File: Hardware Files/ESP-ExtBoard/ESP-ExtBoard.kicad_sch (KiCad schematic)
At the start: 6 parts, among them J1 PIN_HEADER, J2 PIN_HEADER_1x4, U1 ESP32-DEVKIT-V1, U2 BME280, U3 MPU6050, U4 SSD1306

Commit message: Signed-off-by: Freire <freireg1503@gmail.com>
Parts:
- added J3: PIN_HEADER, New_lib:PinHeader_1x06_P2.54mm_Vertical, symbol New_Library:PIN_HEADER_1x6
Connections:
- net +3.3V: now also J3.1
- net Earth: now also J3.2
- net GPIO25: now reaches U1.23 (D25)
- net GPIO25: now also J3.6
- net GPIO26: now reaches U1.24 (D26)
- net GPIO26: now also J3.5
- net GPIO27: now reaches U1.25 (D27)
- net GPIO27: now also J3.4
- net GPIO14: now reaches U1.26 (D14)
- net GPIO14: now also J3.3
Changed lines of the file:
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@@
+    (stroke (width 0) (type default))
+  )
+  (wire (pts (xy 88.9 91.44) (xy 86.36 91.44))
+    (stroke (width 0) (type default))
+  )
+  (wire (pts (xy 115.57 139.7) (xy 118.11 139.7))
+    (stroke (width 0) (type default))
+  )
+  (wire (pts (xy 114.3 149.86) (xy 118.11 149.86))
     (stroke (width 0) (type default))
   )
@@
     (stroke (width 0) (type default))
   )
+  (wire (pts (xy 115.57 147.32) (xy 118.11 147.32))
+    (stroke (width 0) (type default))
+  )
   (wire (pts (xy 114.3 113.03) (xy 118.11 113.03))
     (stroke (width 0) (type default))
   )
+  (wire (pts (xy 52.07 96.52) (xy 55.88 96.52))
+    (stroke (width 0) (type default))
+  )
   (wire (pts (xy 115.57 133.35) (xy 118.11 133.35))
     (stroke (width 0) (type default))
@@
     (stroke (width 0) (type default))
   )
+  (wire (pts (xy 115.57 152.4) (xy 118.11 152.4))
+    (stroke (width 0) (type default))
+  )
   (wire (pts (xy 86.36 115.57) (xy 86.36 111.76))
     (stroke (width 0) (type default))
@@
     (stroke (width 0) (type default))
   )
+  (wire (pts (xy 115.57 142.24) (xy 118.11 142.24))
+    (stroke (width 0) (type default))
+  )
   (wire (pts (xy 114.3 130.81) (xy 118.11 130.81))
     (stroke (width 0) (type default))
@@
     (stroke (width 0) (type default))
   )
+  (wire (pts (xy 88.9 93.98) (xy 86.36 93.98))
+    (stroke (width 0) (type default))
+  )
+  (wire (pts (xy 88.9 88.9) (xy 86.36 88.9))
+    (stroke (width 0) (type default))
+  )
+  (wire (pts (xy 115.57 144.78) (xy 118.11 144.78))
+    (stroke (width 0) (type default))
+  )
   (wire (pts (xy 118.11 92.71) (xy 114.3 92.71))
     (stroke (width 0) (type default))
@@
   (label "VSPI_MISO" (at 115.57 125.73 180) (fields_autoplaced)
     (effects (font (size 1.27 1.27)) (justify right bottom))
+  )
+  (label "GPIO26" (at 88.9 91.44 0) (fields_autoplaced)
+    (effects (font (size 1.27 1.27)) (justify left bottom))
   )
   (label "UART2_RX" (at 88.9 76.2 0) (fields_autoplaced)
@@
     (effects (font (size 1.27 1.27)) (justify right bottom))
   )
+  (label "GPIO14" (at 115.57 147.32 180) (fields_autoplaced)
+    (effects (font (size 1.27 1.27)) (justify right bottom))
+  )
+  (label "GPIO27" (at 88.9 93.98 0) (fields_autoplaced)
+    (effects (font (size 1.27 1.27)) (justify left bottom))
+  )
+  (label "GPIO26" (at 115.57 142.24 180) (fields_autoplaced)
+    (effects (font (size 1.27 1.27)) (justify right bottom))
+  )
   (label "VSPI_CLK" (at 114.3 123.19 180) (fields_autoplaced)
     (effects (font (size 1.27 1.27)) (justify right bottom))
@@
     (effects (font (size 1.27 1.27)) (justify right bottom))
   )
+  (label "GPIO25" (at 88.9 88.9 0) (fields_autoplaced)
+    (effects (font (size 1.27 1.27)) (justify left bottom))
+  )
+  (label "GPIO14" (at 52.07 96.52 180) (fields_autoplaced)
+    (effects (font (size 1.27 1.27)) (justify right bottom))
+  )
   (label "VSPI_MOSI" (at 88.9 86.36 0) (fields_autoplaced)
     (effects (font (size 1.27 1.27)) (justify left bottom))
@@
     (effects (font (size 1.27 1.27)) (justify left bottom))
   )
+  (label "GPIO27" (at 115.57 144.78 180) (fields_autoplaced)
+    (effects (font (size 1.27 1.27)) (justify right bottom))
+  )
   (label "VSPI_CS" (at 50.8 88.9 180) (fields_autoplaced)
     (effects (font (size 1.27 1.27)) (justify right bottom))
@@
   )
   (label "I2C0_SCL" (at 114.3 92.71 180) (fields_autoplaced)
+    (effects (font (size 1.27 1.27)) (justify right bottom))
+  )
+  (label "GPIO25" (at 115.57 139.7 180) (fields_autoplaced)
     (effects (font (size 1.27 1.27)) (justify right bottom))
   )
@@
         (path "/1974cf77-3075-4097-b9ae-5746e4e11ede"
           (reference "U2") (unit 1)
+        )
+      )
+    )
+  )
+  (symbol (lib_id "power:+3.3V") (at 115.57 152.4 90) (unit 1)
+    (in_bom yes) (on_board yes) (dnp no) (fields_autoplaced)
+    (property "Reference" "#PWR014" (at 119.38 152.4 0)
+      (effects (font (size 1.27 1.27)) hide)
+    )
+    (property "Value" "+3.3V" (at 110.49 152.4 0)
+      (effects (font (size 1.27 1.27)))
+    )
+    (property "Footprint" "" (at 115.57 152.4 0)
+      (effects (font (size 1.27 1.27)) hide)
+    )
+    (property "Datasheet" "" (at 115.57 152.4 0)
+      (effects (font (size 1.27 1.27)) hide)
+    )
+    (pin "1")
+    (instances
+      (project "ESP-ExtBoard"
+        (path "/1974cf77-3075-4097-b9ae-5746e4e11ede"
+          (reference "#PWR014") (unit 1)
         )
       )
@@
     )
   )
-  (symbol (lib_id "New_Library:SSD1306") (at 127 109.22 90) (unit 1)
-    (in_bom yes) (on_board yes) (dnp no) (fields_autoplaced)
-    (property "Reference" "U4" (at 134.62 107.95 90)
-      (effects (font (size 1.27 1.27)) (justify right))
-    )
-    (property "Value" "SSD1306" (at 134.62 110.49 90)
-      (effects (font (size 1.27 1.27)) (justify right))
-    )
-    (property "Footprint" "New_lib:128x64OLED" (at 120.65 109.22 0)
-      (effects (font (size 1.27 1.27)) hide)
-    )
-    (property "Datasheet" "" (at 120.65 109.22 0)
+  (symbol (lib_id "New_Library:PIN_HEADER_1x6") (at 124.46 147.32 90) (unit 1)
+    (in_bom yes) (on_board yes) (dnp no) (fields_autoplaced)
+    (property "Reference" "J3" (at 128.27 146.05 90)
+      (effects (font (size 1.27 1.27)) (justify right))
+    )
+    (property "Value" "PIN_HEADER" (at 128.27 148.59 90)
+      (effects (font (size 1.27 1.27)) (justify right))
+    )
+    (property "Footprint" "New_lib:PinHeader_1x06_P2.54mm_Vertical" (at 128.27 148.59 0)
+      (effects (font (size 1.27 1.27)) hide)
+    )
+    (property "Datasheet" "" (at 124.46 148.59 0)
       (effects (font (size 1.27 1.27)) hide)
     )
@@
     (pin "3")
     (pin "4")
+    (pin "5")
+    (pin "6")
+    (instances
+      (project "ESP-ExtBoard"
+        (path "/1974cf77-3075-4097-b9ae-5746e4e11ede"
+          (reference "J3") (unit 1)
+        )
+      )
+    )
+  )
+  (symbol (lib_id "New_Library:SSD1306") (at 127 109.22 90) (unit 1)
+    (in_bom yes) (on_board yes) (dnp no) (fields_autoplaced)
+    (property "Reference" "U4" (at 134.62 107.95 90)
+      (effects (font (size 1.27 1.27)) (justify right))
+    )
+    (property "Value" "SSD1306" (at 134.62 110.49 90)
+      (effects (font (size 1.27 1.27)) (justify right))
+    )
+    (property "Footprint" "New_lib:128x64OLED" (at 120.65 109.22 0)
+      (effects (font (size 1.27 1.27)) hide)
+    )
+    (property "Datasheet" "" (at 120.65 109.22 0)
+      (effects (font (size 1.27 1.27)) hide)
+    )
+    (pin "1")
+    (pin "2")
+    (pin "3")
+    (pin "4")
     (instances
       (project "ESP-ExtBoard"
@@
         )
       )
+    )
+  )
+  (symbol (lib_id "power:Earth") (at 114.3 149.86 270) (unit 1)
+    (in_bom yes) (on_board yes) (dnp no) (fields_autoplaced)
+    (property "Reference" "#PWR013" (at 107.95 149.86 0)
+      (effects (font (size 1.27 1.27)) hide)
+    )
+    (property "Value" "Earth" (at 110.49 149.86 0)
+      (effects (font (size 1.27 1.27)) hide)
+    )
+    (property "Footprint" "" (at 114.3 149.86 0)
+      (effects (font (size 1.27 1.27)) hide)
+    )
+    (property "Datasheet" "~" (at 114.3 149.86 0)
+      (effects (font (size 1.27 1.27)) hide)
+    )
+    (pin "1")
+    (instances
+      (project "ESP-ExtBoard"
+        (path "/1974cf77-3075-4097-b9ae-5746e4e11ede"
+          (reference "#PWR013") (unit 1)
+        )
+      )

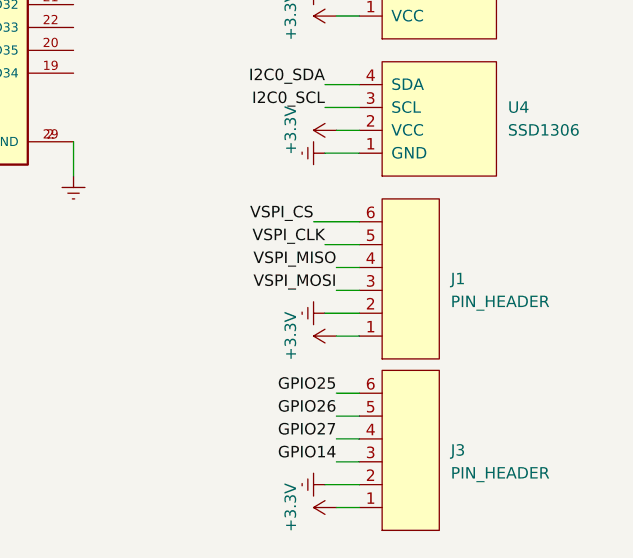
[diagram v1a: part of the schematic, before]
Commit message: [hardware] SD module pin update
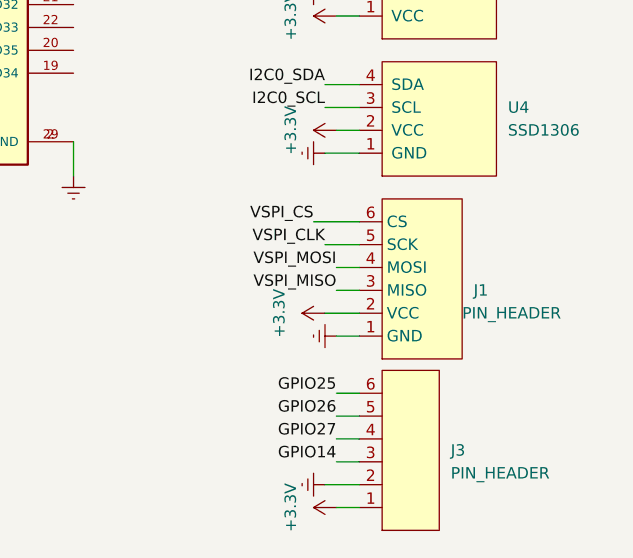
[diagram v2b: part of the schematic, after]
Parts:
- J1: footprint New_lib:PinHeader_1x06_P2.54mm_Vertical -> New_lib:PinHeader_1x06_P2.54mm_Vertical_1; symbol New_Library:PIN_HEADER_1x6 -> New_Library:SD_Module
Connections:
- net +3.3V: now also J1.2 (VCC); no longer J1.1
- net Earth: now also J1.1 (GND); no longer J1.2
- net VSPI_MISO: now also J1.3 (MISO); no longer J1.4
- net VSPI_MOSI: now also J1.4 (MOSI); no longer J1.3
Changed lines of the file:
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@@
     (stroke (width 0) (type default))
   )
-  (label "VSPI_MISO" (at 115.57 125.73 180) (fields_autoplaced)
-    (effects (font (size 1.27 1.27)) (justify right bottom))
-  )
   (label "GPIO26" (at 88.9 91.44 0) (fields_autoplaced)
     (effects (font (size 1.27 1.27)) (justify left bottom))
@@
     (effects (font (size 1.27 1.27)) (justify left bottom))
   )
+  (label "VSPI_MOSI" (at 115.57 125.73 180) (fields_autoplaced)
+    (effects (font (size 1.27 1.27)) (justify right bottom))
+  )
   (label "GPIO26" (at 115.57 142.24 180) (fields_autoplaced)
     (effects (font (size 1.27 1.27)) (justify right bottom))
@@
     (effects (font (size 1.27 1.27)) (justify right bottom))
   )
-  (label "VSPI_MOSI" (at 115.57 128.27 180) (fields_autoplaced)
-    (effects (font (size 1.27 1.27)) (justify right bottom))
-  )
   (label "UART2_RX" (at 115.57 52.07 180) (fields_autoplaced)
     (effects (font (size 1.27 1.27)) (justify right bottom))
@@
     (effects (font (size 1.27 1.27)) (justify right bottom))
   )
+  (label "VSPI_MISO" (at 115.57 128.27 180) (fields_autoplaced)
+    (effects (font (size 1.27 1.27)) (justify right bottom))
+  )
   (label "I2C0_SCL" (at 114.3 107.95 180) (fields_autoplaced)
     (effects (font (size 1.27 1.27)) (justify right bottom))
@@
   (label "UART2_TX" (at 115.57 49.53 180) (fields_autoplaced)
     (effects (font (size 1.27 1.27)) (justify right bottom))
-  )
-  (symbol (lib_id "power:Earth") (at 114.3 130.81 270) (unit 1)
-    (in_bom yes) (on_board yes) (dnp no) (fields_autoplaced)
-    (property "Reference" "#PWR09" (at 107.95 130.81 0)
-      (effects (font (size 1.27 1.27)) hide)
-    )
-    (property "Value" "Earth" (at 110.49 130.81 0)
-      (effects (font (size 1.27 1.27)) hide)
-    )
-    (property "Footprint" "" (at 114.3 130.81 0)
-      (effects (font (size 1.27 1.27)) hide)
-    )
-    (property "Datasheet" "~" (at 114.3 130.81 0)
-      (effects (font (size 1.27 1.27)) hide)
-    )
-    (pin "1")
-    (instances
-      (project "ESP-ExtBoard"
-        (path "/1974cf77-3075-4097-b9ae-5746e4e11ede"
-          (reference "#PWR09") (unit 1)
-        )
-      )
-    )
   )
   (symbol (lib_id "New_Library:PIN_HEADER_1x4") (at 124.46 52.07 90) (unit 1)
@@
     )
   )
-  (symbol (lib_id "New_Library:PIN_HEADER_1x6") (at 124.46 128.27 90) (unit 1)
-    (in_bom yes) (on_board yes) (dnp no) (fields_autoplaced)
-    (property "Reference" "J1" (at 128.27 127 90)
-      (effects (font (size 1.27 1.27)) (justify right))
-    )
-    (property "Value" "PIN_HEADER" (at 128.27 129.54 90)
-      (effects (font (size 1.27 1.27)) (justify right))
-    )
-    (property "Footprint" "New_lib:PinHeader_1x06_P2.54mm_Vertical" (at 128.27 129.54 0)
+  (symbol (lib_id "New_Library:SD_Module") (at 124.46 128.27 90) (unit 1)
+    (in_bom yes) (on_board yes) (dnp no)
+    (property "Reference" "J1" (at 130.81 128.27 90)
+      (effects (font (size 1.27 1.27)) (justify right))
+    )
+    (property "Value" "PIN_HEADER" (at 129.54 130.81 90)
+      (effects (font (size 1.27 1.27)) (justify right))
+    )
+    (property "Footprint" "New_lib:PinHeader_1x06_P2.54mm_Vertical_1" (at 128.27 129.54 0)
       (effects (font (size 1.27 1.27)) hide)
     )
@@
         (path "/1974cf77-3075-4097-b9ae-5746e4e11ede"
           (reference "#PWR06") (unit 1)
+        )
+      )
+    )
+  )
+  (symbol (lib_id "power:+3.3V") (at 114.3 130.81 90) (unit 1)
+    (in_bom yes) (on_board yes) (dnp no) (fields_autoplaced)
+    (property "Reference" "#PWR010" (at 118.11 130.81 0)
+      (effects (font (size 1.27 1.27)) hide)
+    )
+    (property "Value" "+3.3V" (at 109.22 130.81 0)
+      (effects (font (size 1.27 1.27)))
+    )
+    (property "Footprint" "" (at 114.3 130.81 0)
+      (effects (font (size 1.27 1.27)) hide)
+    )
+    (property "Datasheet" "" (at 114.3 130.81 0)
+      (effects (font (size 1.27 1.27)) hide)
+    )
+    (pin "1")
+    (instances
+      (project "ESP-ExtBoard"
+        (path "/1974cf77-3075-4097-b9ae-5746e4e11ede"
+          (reference "#PWR010") (unit 1)
         )
       )
@@
     )
   )
+  (symbol (lib_id "power:Earth") (at 115.57 133.35 270) (unit 1)
+    (in_bom yes) (on_board yes) (dnp no) (fields_autoplaced)
+    (property "Reference" "#PWR09" (at 109.22 133.35 0)
+      (effects (font (size 1.27 1.27)) hide)
+    )
+    (property "Value" "Earth" (at 111.76 133.35 0)
+      (effects (font (size 1.27 1.27)) hide)
+    )
+    (property "Footprint" "" (at 115.57 133.35 0)
+      (effects (font (size 1.27 1.27)) hide)
+    )
+    (property "Datasheet" "~" (at 115.57 133.35 0)
+      (effects (font (size 1.27 1.27)) hide)
+    )
+    (pin "1")
+    (instances
+      (project "ESP-ExtBoard"
+        (path "/1974cf77-3075-4097-b9ae-5746e4e11ede"
+          (reference "#PWR09") (unit 1)
+        )
+      )
+    )
+  )
   (symbol (lib_id "power:+3.3V") (at 115.57 97.79 90) (unit 1)
     (in_bom yes) (on_board yes) (dnp no) (fields_autoplaced)
@@
         )
       )
-    )
-  )
-  (symbol (lib_id "power:+3.3V") (at 115.57 133.35 90) (unit 1)
-    (in_bom yes) (on_board yes) (dnp no) (fields_autoplaced)
-    (property "Reference" "#PWR010" (at 119.38 133.35 0)
-      (effects (font (size 1.27 1.27)) hide)
-    )
-    (property "Value" "+3.3V" (at 110.49 133.35 0)
-      (effects (font (size 1.27 1.27)))
-    )
-    (property "Footprint" "" (at 115.57 133.35 0)
-      (effects (font (size 1.27 1.27)) hide)
-    )
-    (property "Datasheet" "" (at 115.57 133.35 0)
-      (effects (font (size 1.27 1.27)) hide)
-    )
-    (pin "1")
-    (instances
-      (project "ESP-ExtBoard"
-        (path "/1974cf77-3075-4097-b9ae-5746e4e11ede"
-          (reference "#PWR010") (unit 1)
-        )
-      )

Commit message: [hardware] minor updates
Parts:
- added J4: PIN_HEADER, New_lib:PinHeader_1x06_P2.54mm_Vertical, symbol New_Library:PIN_HEADER_1x6
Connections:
- net Earth: now also J4.2
- net GPIO34: now reaches U1.19 (D34)
- net GPIO34: now also J4.3
- net GPIO35: now reaches U1.20 (D35)
- net GPIO35: now also J4.4
- net GPIO32: now reaches U1.21 (D32)
- net GPIO32: now also J4.5
- net GPIO33: now reaches U1.22 (D33)
- net GPIO33: now also J4.6
- net +5V: now reaches U1.30 (VIN)
- net +5V: now also J4.1
